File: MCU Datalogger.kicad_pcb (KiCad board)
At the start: 2 copper layers, 51.4 x 34.3 mm, 31 parts, among them J1 Conn_01x04_Male, J2 Conn_01x09_Male, J3 Conn_01x04_Male, J4 Conn_02x03_Odd_Even, U1 24LC1025, U2 DS1337S+, U3 24LC1025, U4 ATMEGA328P-AU, Y1 32.768 KHz, Y2 16 MHz

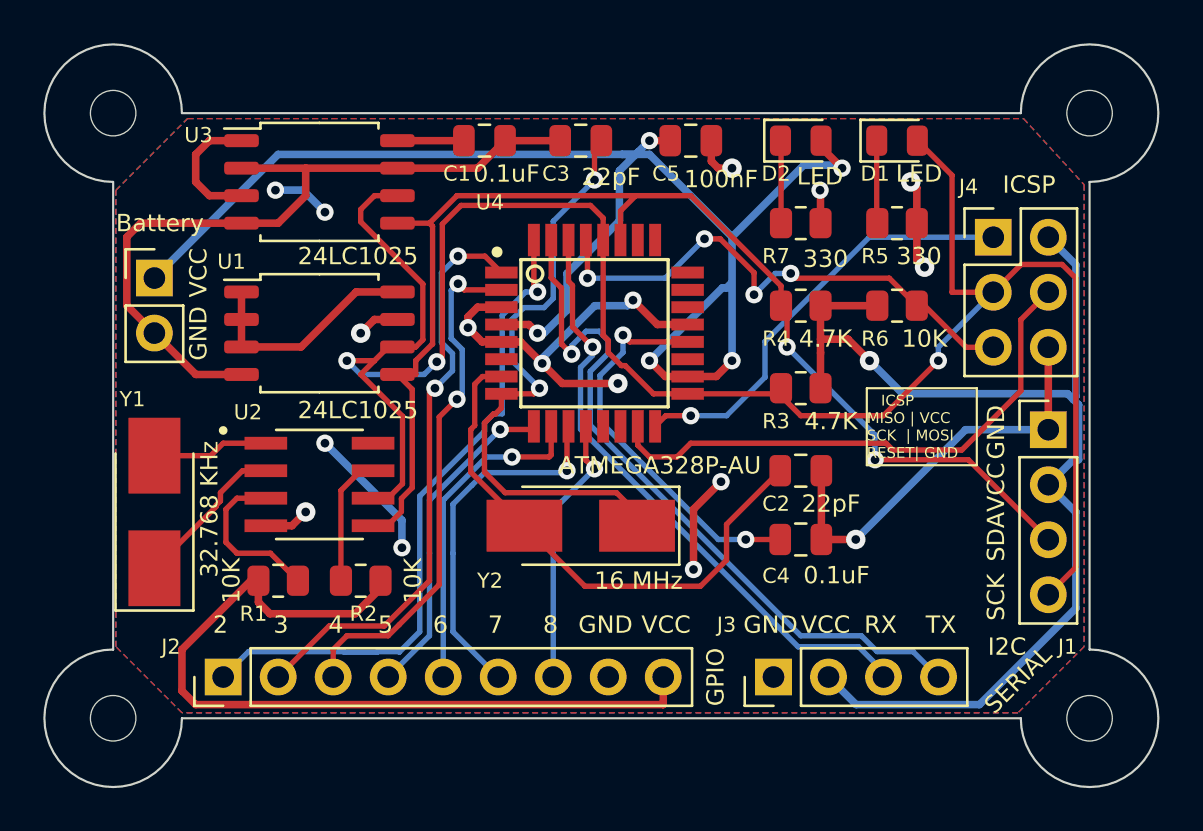
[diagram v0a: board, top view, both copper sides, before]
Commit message: Unrouted 2-layer board.
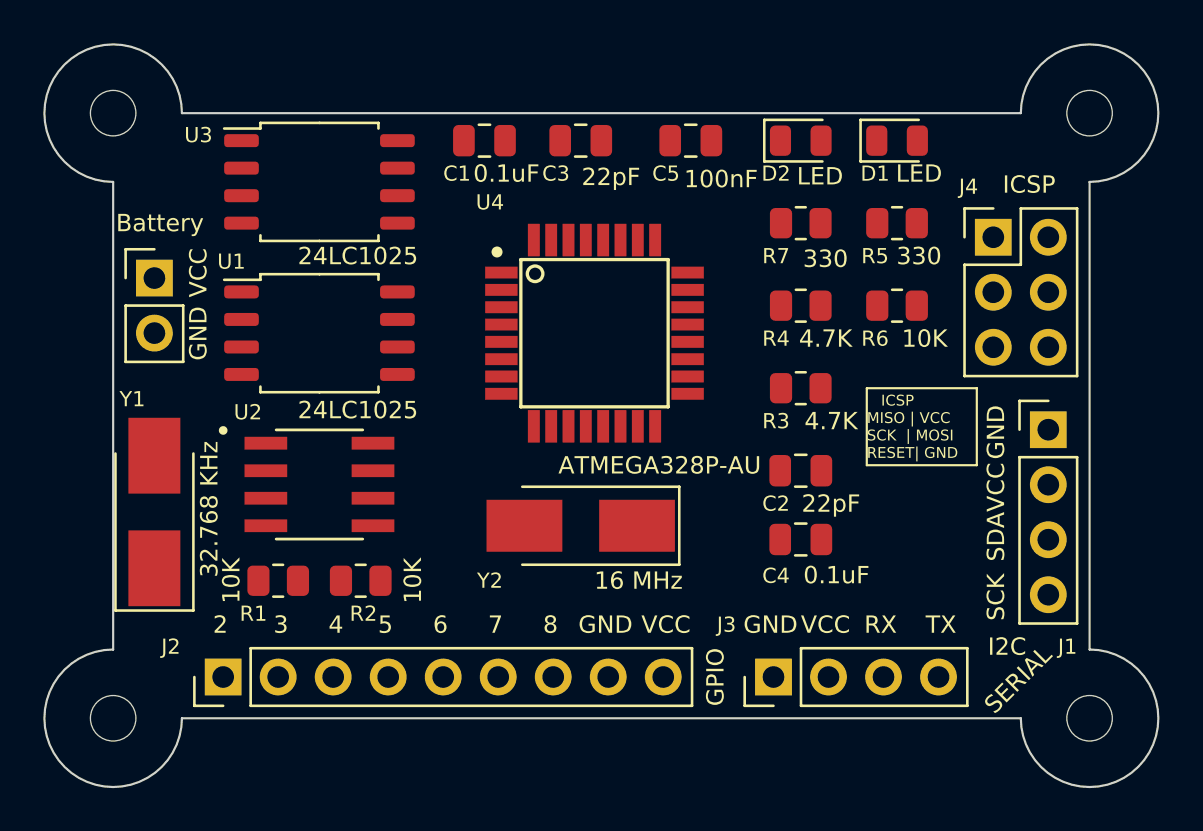
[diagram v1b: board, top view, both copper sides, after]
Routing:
- net /Vcc: track 188.4 -> 0.00 mm, vias 10 -> 0
- net /SCK: track 98.0 -> 0.00 mm, vias 3 -> 0
- net GND: track 90.4 -> 0.00 mm, vias 13 -> 0
- net /SDA: track 58.3 -> 0.00 mm, vias 2 -> 0
- net /TX: track 33.3 -> 0.00 mm, vias 1 -> 0
- net /D2: track 30.9 -> 0.00 mm, vias 1 -> 0
- net Net-(Y2-Pad1): track 28.8 -> 0.00 mm, vias 2 -> 0
- net /RX: track 28.3 -> 0.00 mm, vias 1 -> 0
- net /D3: track 27.2 -> 0.00 mm, vias 2 -> 0
- net /MOSI: track 25.4 -> 0.00 mm
- net Net-(Y2-Pad2): track 25.2 -> 0.00 mm
- net /RESET: track 24.8 -> 0.00 mm, vias 4 -> 0
- net /D4: track 24.2 -> 0.00 mm, vias 2 -> 0
- net /MISO: track 20.2 -> 0.00 mm, vias 1 -> 0
- net Net-(U4-Pad20): track 18.1 -> 0.00 mm, vias 2 -> 0
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- removed copper zone on F.Cu, net /Vcc
- removed copper zone on B.Cu, net GND

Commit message: Added automaticaly routed 2-layer board.
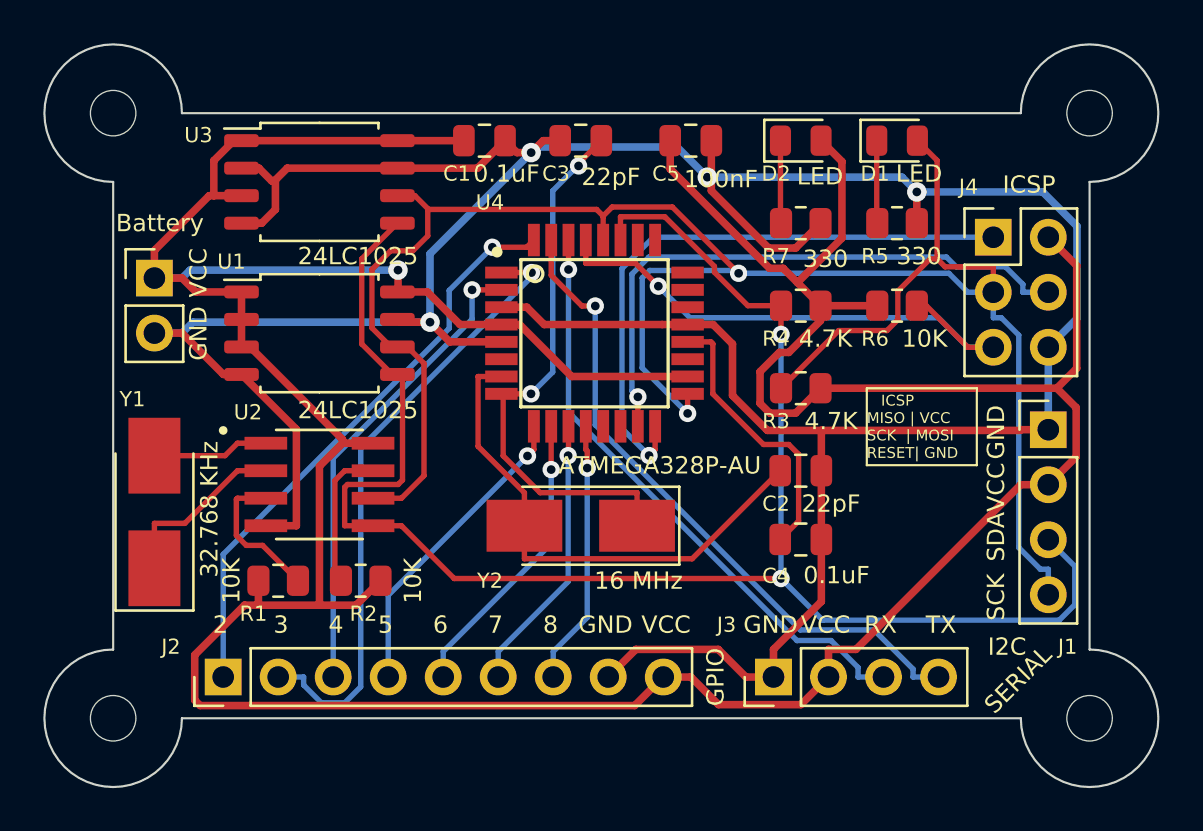
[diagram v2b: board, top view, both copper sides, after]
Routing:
- net /Vcc: track 0.00 -> 183.7 mm, vias 0 -> 1
- net GND: track 0.00 -> 158.8 mm, vias 0 -> 4
- net /SCK: track 0.00 -> 97.4 mm, vias 0 -> 2
- net /SDA: track 0.00 -> 80.3 mm, vias 0 -> 2
- net /TX: track 0.00 -> 30.6 mm, vias 0 -> 1
- net /D3: track 0.00 -> 28.6 mm, vias 0 -> 1
- net /MISO: track 0.00 -> 28.4 mm, vias 0 -> 1
- net /RX: track 0.00 -> 27.8 mm, vias 0 -> 1
- net /MOSI: track 0.00 -> 27.6 mm, vias 0 -> 1
- net /D2: track 0.00 -> 27.0 mm, vias 0 -> 1
- net /RESET: track 0.00 -> 25.8 mm, vias 0 -> 1
- net Net-(Y2-Pad1): track 0.00 -> 25.7 mm, vias 0 -> 2
- net Net-(Y2-Pad2): track 0.00 -> 23.9 mm
- net /D4: track 0.00 -> 21.9 mm, vias 0 -> 1
- net /D5: track 0.00 -> 14.4 mm, vias 0 -> 1
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
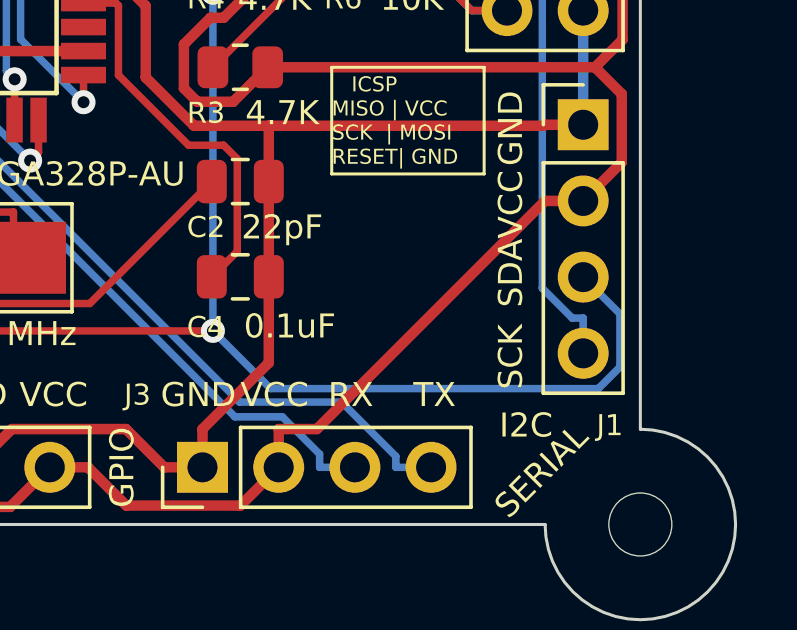
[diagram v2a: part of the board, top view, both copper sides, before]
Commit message: Replaced straigh track with jagged track.
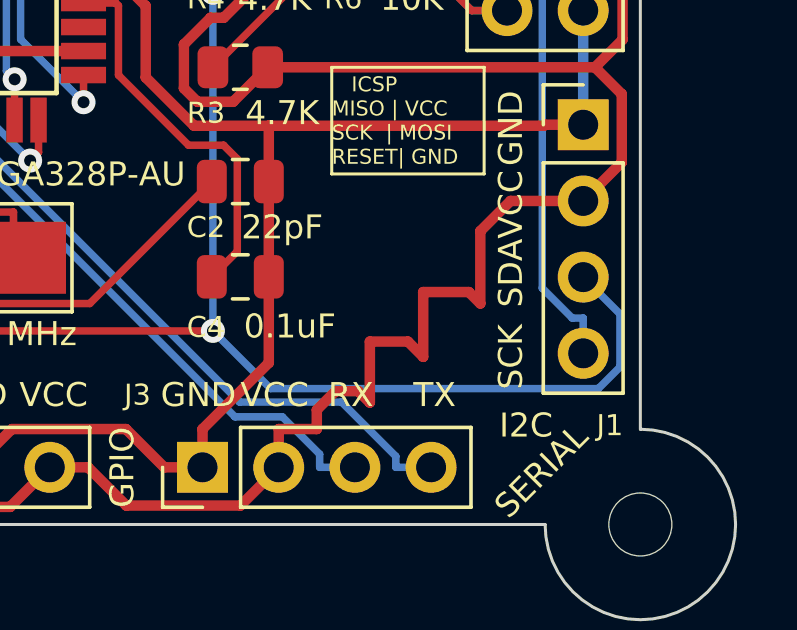
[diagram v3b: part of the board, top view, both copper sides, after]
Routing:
- net /Vcc: track 183.7 -> 189.0 mm
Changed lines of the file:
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@@
   (segment (start 124.7375 84.514) (end 124.7375 83.82) (width 0.35) (layer "F.Cu") (net 2))
   (segment (start 122.3831 82.0941) (end 123.0116 82.0941) (width 0.35) (layer "F.Cu") (net 2))
+  (segment (start 131.826 93.091) (end 132.832 92.085) (width 0.35) (layer "F.Cu") (net 2))
   (segment (start 105.2271 83.1579) (end 105.2 83.185) (width 0.35) (layer "F.Cu") (net 2))
+  (segment (start 127 98.425) (end 127.762 98.425) (width 0.35) (layer "F.Cu") (net 2))
+  (segment (start 128.143 98.806) (end 128.143 96.774) (width 0.35) (layer "F.Cu") (net 2))
   (segment (start 98 83.185) (end 95.8953 83.185) (width 0.35) (layer "F.Cu") (net 2))
   (segment (start 120.0257 102.2404) (end 123.8296 102.2404) (width 0.35) (layer "F.Cu") (net 2))
   (segment (start 103.2872 97.6503) (end 104.4175 96.52) (width 0.35) (layer "F.Cu") (net 2))
   (segment (start 98 85.725) (end 98 84.455) (width 0.35) (layer "F.Cu") (net 2))
+  (segment (start 128.143 96.774) (end 129.413 96.774) (width 0.35) (layer "F.Cu") (net 2))
   (segment (start 101.6 91.2347) (end 102.6647 90.17) (width 0.35) (layer "F.Cu") (net 2))
   (segment (start 124.7375 87.63) (end 123.5867 88.7808) (width 0.35) (layer "F.Cu") (net 2))
@@
   (segment (start 95.8403 99.9486) (end 95.8403 102.032) (width 0.35) (layer "F.Cu") (net 2))
   (segment (start 136.5396 90.8004) (end 136.5396 88.5225) (width 0.35) (layer "F.Cu") (net 2))
+  (segment (start 127.762 98.425) (end 128.143 98.806) (width 0.35) (layer "F.Cu") (net 2))
+  (segment (start 126.375 99.6897) (end 126.375 99.05) (width 0.35) (layer "F.Cu") (net 2))
   (segment (start 95.8403 102.032) (end 96.0919 102.2836) (width 0.35) (layer "F.Cu") (net 2))
   (segment (start 96.0919 102.2836) (end 116.1564 102.2836) (width 0.35) (layer "F.Cu") (net 2))
@@
   (segment (start 136.566 81.971) (end 136.566 86.7111) (width 0.35) (layer "F.Cu") (net 2))
   (segment (start 117.795 76.2) (end 117.795 77.506) (width 0.35) (layer "F.Cu") (net 2))
+  (segment (start 129.921 95.123) (end 131.445 95.123) (width 0.35) (layer "F.Cu") (net 2))
+  (segment (start 132.832 92.085) (end 135.255 92.085) (width 0.35) (layer "F.Cu") (net 2))
   (segment (start 106.5848 83.185) (end 108.0898 84.69) (width 0.35) (layer "F.Cu") (net 2))
   (segment (start 96.7226 78.74) (end 96.5097 78.74) (width 0.35) (layer "F.Cu") (net 2))
@@
   (segment (start 102.6647 90.17) (end 102.6647 89.9899) (width 0.35) (layer "F.Cu") (net 2))
   (segment (start 127.3575 83.82) (end 124.7375 83.82) (width 0.35) (layer "F.Cu") (net 2))
+  (segment (start 129.413 96.774) (end 129.921 97.282) (width 0.35) (layer "F.Cu") (net 2))
   (segment (start 123.6712 82.7537) (end 125.7262 80.6987) (width 0.35) (layer "F.Cu") (net 2))
   (segment (start 98 84.455) (end 98 83.185) (width 0.35) (layer "F.Cu") (net 2))
+  (segment (start 131.445 95.123) (end 131.826 95.504) (width 0.35) (layer "F.Cu") (net 2))
   (segment (start 98.1427 97.6462) (end 95.8403 99.9486) (width 0.35) (layer "F.Cu") (net 2))
   (segment (start 95.8953 83.185) (end 95.2553 82.545) (width 0.35) (layer "F.Cu") (net 2))
   (segment (start 108.27 76.2) (end 105.2 76.2) (width 0.35) (layer "F.Cu") (net 2))
+  (segment (start 129.921 97.282) (end 129.921 95.123) (width 0.35) (layer "F.Cu") (net 2))
   (segment (start 117.795 77.506) (end 122.3831 82.0941) (width 0.35) (layer "F.Cu") (net 2))
   (segment (start 116.1564 102.2836) (end 117.475 100.965) (width 0.35) (layer "F.Cu") (net 2))
@@
   (segment (start 118.6 87.09) (end 113.246 87.09) (width 0.35) (layer "F.Cu") (net 2))
   (segment (start 123.2724 85.9791) (end 124.7375 84.514) (width 0.35) (layer "F.Cu") (net 2))
-  (segment (start 126.375 99.6897) (end 133.9797 92.085) (width 0.35) (layer "F.Cu") (net 2))
+  (segment (start 131.826 95.504) (end 131.826 93.091) (width 0.35) (layer "F.Cu") (net 2))
   (segment (start 135.255 92.085) (end 136.5396 90.8004) (width 0.35) (layer "F.Cu") (net 2))
   (segment (start 123.8296 102.2404) (end 125.105 100.965) (width 0.35) (layer "F.Cu") (net 2))
@@
   (segment (start 104.075 90.17) (end 102.6647 90.17) (width 0.35) (layer "F.Cu") (net 2))
   (segment (start 98.7825 96.52) (end 98.7825 97.6462) (width 0.35) (layer "F.Cu") (net 2))
+  (segment (start 126.375 99.05) (end 127 98.425) (width 0.35) (layer "F.Cu") (net 2))
   (segment (start 98.3998 85.725) (end 98 85.725) (width 0.35) (layer "F.Cu") (net 2))
   (segment (start 125.105 100.965) (end 125.105 99.6897) (width 0.35) (layer "F.Cu") (net 2))
@@
   (segment (start 93.98 82.545) (end 95.2553 82.545) (width 0.35) (layer "F.Cu") (net 2))
   (segment (start 113.246 87.09) (end 110.846 84.69) (width 0.35) (layer "F.Cu") (net 2))
-  (segment (start 135.255 92.085) (end 133.9797 92.085) (width 0.35) (layer "F.Cu") (net 2))
   (via (at 105.2271 82.1769) (size 0.9) (drill 0.4) (layers "F.Cu" "B.Cu") (net 2))
   (segment (start 95.6234 82.1769) (end 105.2271 82.1769) (width 0.35) (layer "B.Cu") (net 2))
